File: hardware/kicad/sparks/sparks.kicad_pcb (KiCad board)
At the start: 2 copper layers, 66 x 101 mm, 43 parts, among them J1 Conn_02x04_Odd_Even, J2 TP4056 Breakout, SW1 SW_Push, U1 MAX7219, U2 ESP32-C3-SuperMini

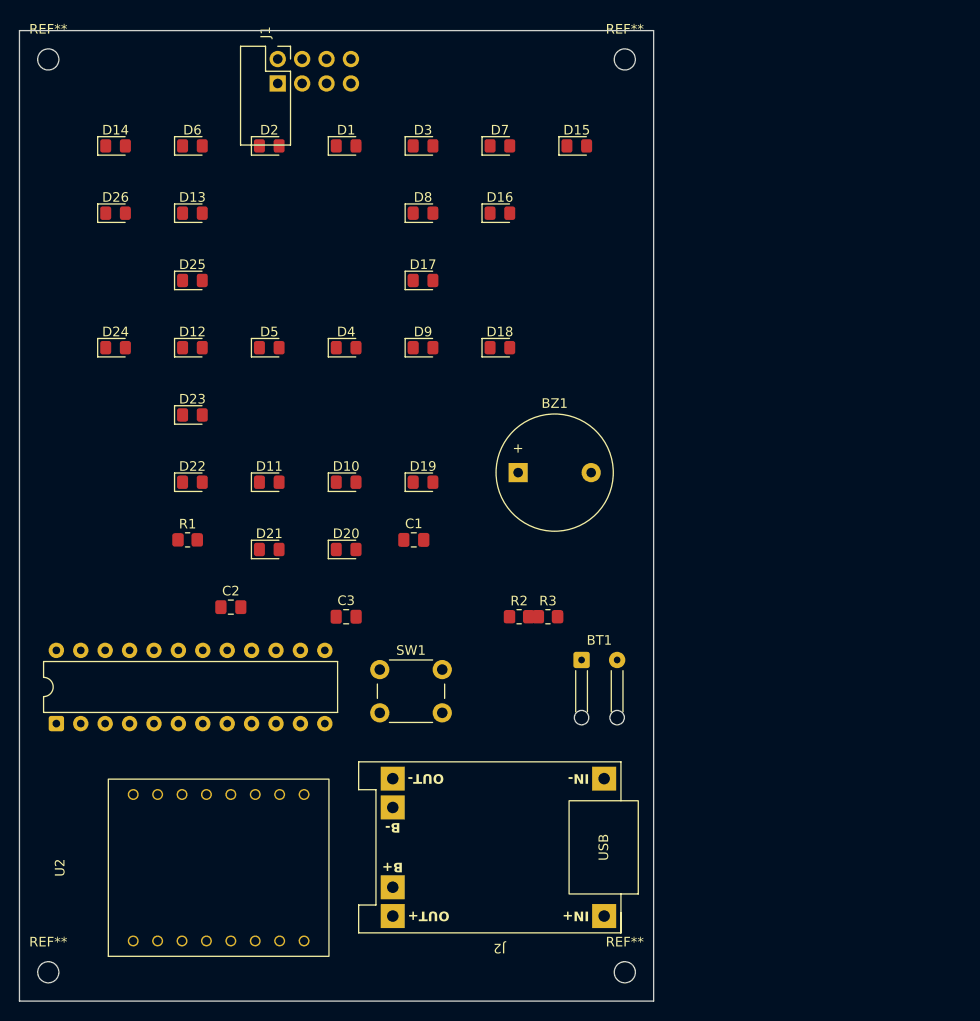
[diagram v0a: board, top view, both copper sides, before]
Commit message: Use a stock pin header for the CC1101 socket, and route DIG0
Replace the CC1101 connector with the stock
PinHeader_2x04_P2.54mm_Vertical at 90 degrees, which gives the
module's own pin arrangement directly: the top row, away from the
board, is 2 4 6 8 and the bottom row, against the board, is
1 3 5 7, with pin 1 on GND and pin 2 on 3V3.

Drop the custom footprint added earlier. It was built on the
assumption that no rotation of a stock part could produce this
layout, which came from testing rotations of the socket footprint
rather than the header - the two number their pads differently.

Route the first track: D1 to D2 on DIG0, 0.4 mm on the front
layer, 9 mm of copper over three segments. The rest of that net
still needs a via down to the MAX7219 on the back.
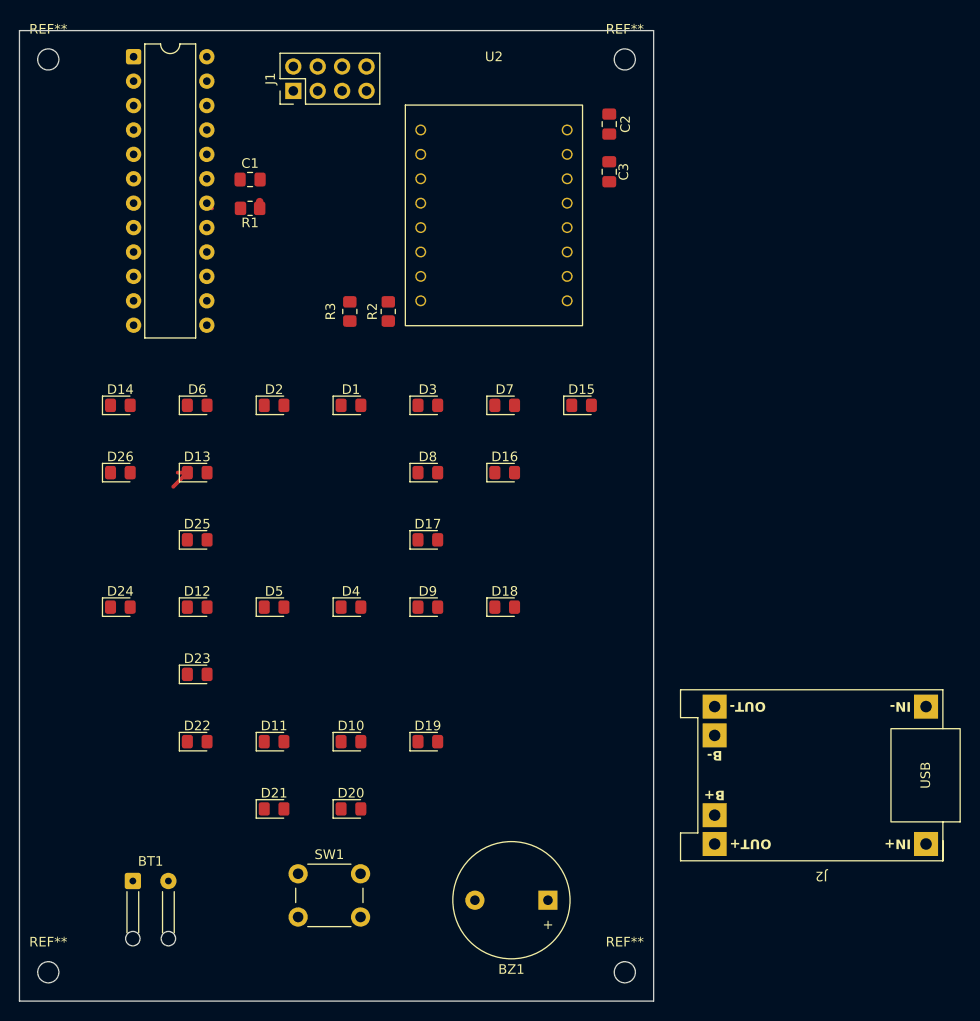
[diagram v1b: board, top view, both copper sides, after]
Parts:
- J1: footprint Sparks:CC1101_Socket_2x04 -> Connector_PinHeader_2.54mm:PinHeader_2x04_P2.54mm_Vertical
- moved U2 73.7 mm to (158.9, 60.7), turned to 0 degrees
- moved U1 69.9 mm to (121.4, 44.2), turned to 0 degrees
- moved C2 63.9 mm to (170.9, 51.2), turned to -90 degrees
- moved C3 53.8 mm to (170.9, 56.2), turned to 90 degrees
- moved BT1 52.1 mm to (121.3, 130.0)
- moved BZ1 44.6 mm to (164.5, 132.0), turned to 180 degrees
- moved C1 41.2 mm to (133.5, 57.0)
- moved R3 37.9 mm to (143.9, 70.7), turned to -90 degrees
- moved R1 35.1 mm to (133.5, 60.0), turned to 180 degrees
- moved R2 34.6 mm to (147.9, 70.7), turned to 90 degrees
- moved J2 34.3 mm to (193.0, 119.0)
- moved D1 27.0 mm to (144.0, 80.5)
- moved D10 27.0 mm to (144.0, 115.5)
- moved D11 27.0 mm to (136.0, 115.5)
- moved D12 27.0 mm to (128.0, 101.5)
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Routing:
- net /DIG2: track 0.00 -> 3.09 mm
- net +5V: track 0.00 -> 1.08 mm
- net Net-(U1-ISET): track 0.00 -> 0.76 mm

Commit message: Clear all routing ahead of autorouting
Remove 177 track segments and 15 vias. Placement, the ground pour,
the board outline and all 45 footprints are untouched.

Manual routing of the matrix proved impractical: the LEDs are
arranged by the Morse tree's geometry while the nets are grouped by
tree level, so same-net LEDs sit far apart and every net has to
weave through the others. Freerouting will be given the clean board
instead.

This commit is the placement-complete, unrouted state, tagged so it
can be returned to if the autorouted result is unsatisfactory.
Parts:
- removed BT1: Battery_Cell, Connector_Wire:SolderWire-0.127sqmm_1x02_P3.7mm_D0.48mm_OD1mm_Relief
- removed J2: TP4056 Breakout, TP4056-Breakout:TP4056-Breakout
- added TP1: BAT+, TestPoint:TestPoint_THTPad_2.0x2.0mm_Drill1.0mm, F.Cu at (158.5, 74.4)
- added TP2: BAT-, TestPoint:TestPoint_THTPad_2.0x2.0mm_Drill1.0mm, F.Cu at (146.5, 74.4)
- added TP3: +5V, TestPoint:TestPoint_THTPad_2.0x2.0mm_Drill1.0mm, F.Cu at (128.0, 54.5)
- added TP4: GND, TestPoint:TestPoint_THTPad_2.0x2.0mm_Drill1.0mm, F.Cu at (128.0, 58.0)
- C2: value 10n -> 10u
- U1: footprint Package_DIP:DIP-24_W7.62mm -> Package_SO:SOIC-24W_7.5x15.4mm_P1.27mm
- moved U1 50.2 mm to (139.5, 91.0), turned to 90 degrees
- moved C2 40.9 mm to (144.0, 82.0), turned to 90 degrees
- moved C3 34.2 mm to (137.0, 51.5), turned to 180 degrees
- moved C1 26.2 mm to (141.5, 82.0), turned to 90 degrees
- moved R1 22.7 mm to (139.0, 82.0), turned to 90 degrees
- moved U2 16.7 mm to (142.3, 62.5), turned to 90 degrees
- moved R3 8.45 mm to (151.5, 74.4)
- moved R2 8.00 mm to (155.0, 74.4)
- moved BZ1 3.47 mm to (162.1, 129.5)
- moved J1 1.20 mm to (138.9, 48.5)
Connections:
- R2 pad 1: /B+ -> /BAT+
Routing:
- net /DIG2: track 3.09 -> 0.00 mm
- net +5V: track 1.08 -> 0.00 mm
- net Net-(U1-ISET): track 0.76 -> 0.00 mm
- added copper zone on B.Cu, net GND

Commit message: Autoroute the board
Route all 29 nets with Freerouting: 391 segments, 1476 mm of copper
and 49 vias across both layers, with no unrouted nets and no
clearance violations.

Manual routing had stalled because the LEDs are positioned by the
Morse tree's geometry while the nets are grouped by tree level, so
same-net LEDs sit far apart and each net has to weave through the
others.

Widen the last 0.3 mm segments left over from hand routing to the
0.4 mm minimum, and narrow the ground pour's thermal spokes to
0.35 mm so every GND pad forms a complete two-spoke relief. DRC
passes.
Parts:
- renumbered REF** to H1, REF** to H2, REF** to H3, REF** to H4
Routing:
- net /DIG2: track 0.00 -> 115.0 mm, vias 0 -> 8
- net /SEG0: track 0.00 -> 114.1 mm, vias 0 -> 1
- net Net-(U2-GPIO10): track 0.00 -> 101.8 mm
- net /DIG3: track 0.00 -> 95.0 mm, vias 0 -> 2
- net /SEG3: track 0.00 -> 93.5 mm, vias 0 -> 2
- net /SEG4: track 0.00 -> 88.8 mm, vias 0 -> 4
- net /SEG7: track 0.00 -> 87.5 mm, vias 0 -> 2
- net /SEG1: track 0.00 -> 81.0 mm, vias 0 -> 4
- net /DIG4: track 0.00 -> 74.9 mm, vias 0 -> 1
- net /SEG6: track 0.00 -> 72.6 mm, vias 0 -> 3
- net Net-(BZ1-+): track 0.00 -> 65.4 mm
- net /SEG2: track 0.00 -> 62.8 mm, vias 0 -> 3
- net /DIG1: track 0.00 -> 58.0 mm, vias 0 -> 4
- net +5V: track 0.00 -> 50.9 mm, vias 0 -> 2
- net /DIG0: track 0.00 -> 41.2 mm, vias 0 -> 3
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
